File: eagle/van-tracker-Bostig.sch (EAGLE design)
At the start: 13 parts, among them K1 CP1-12V, Q1 TIP122

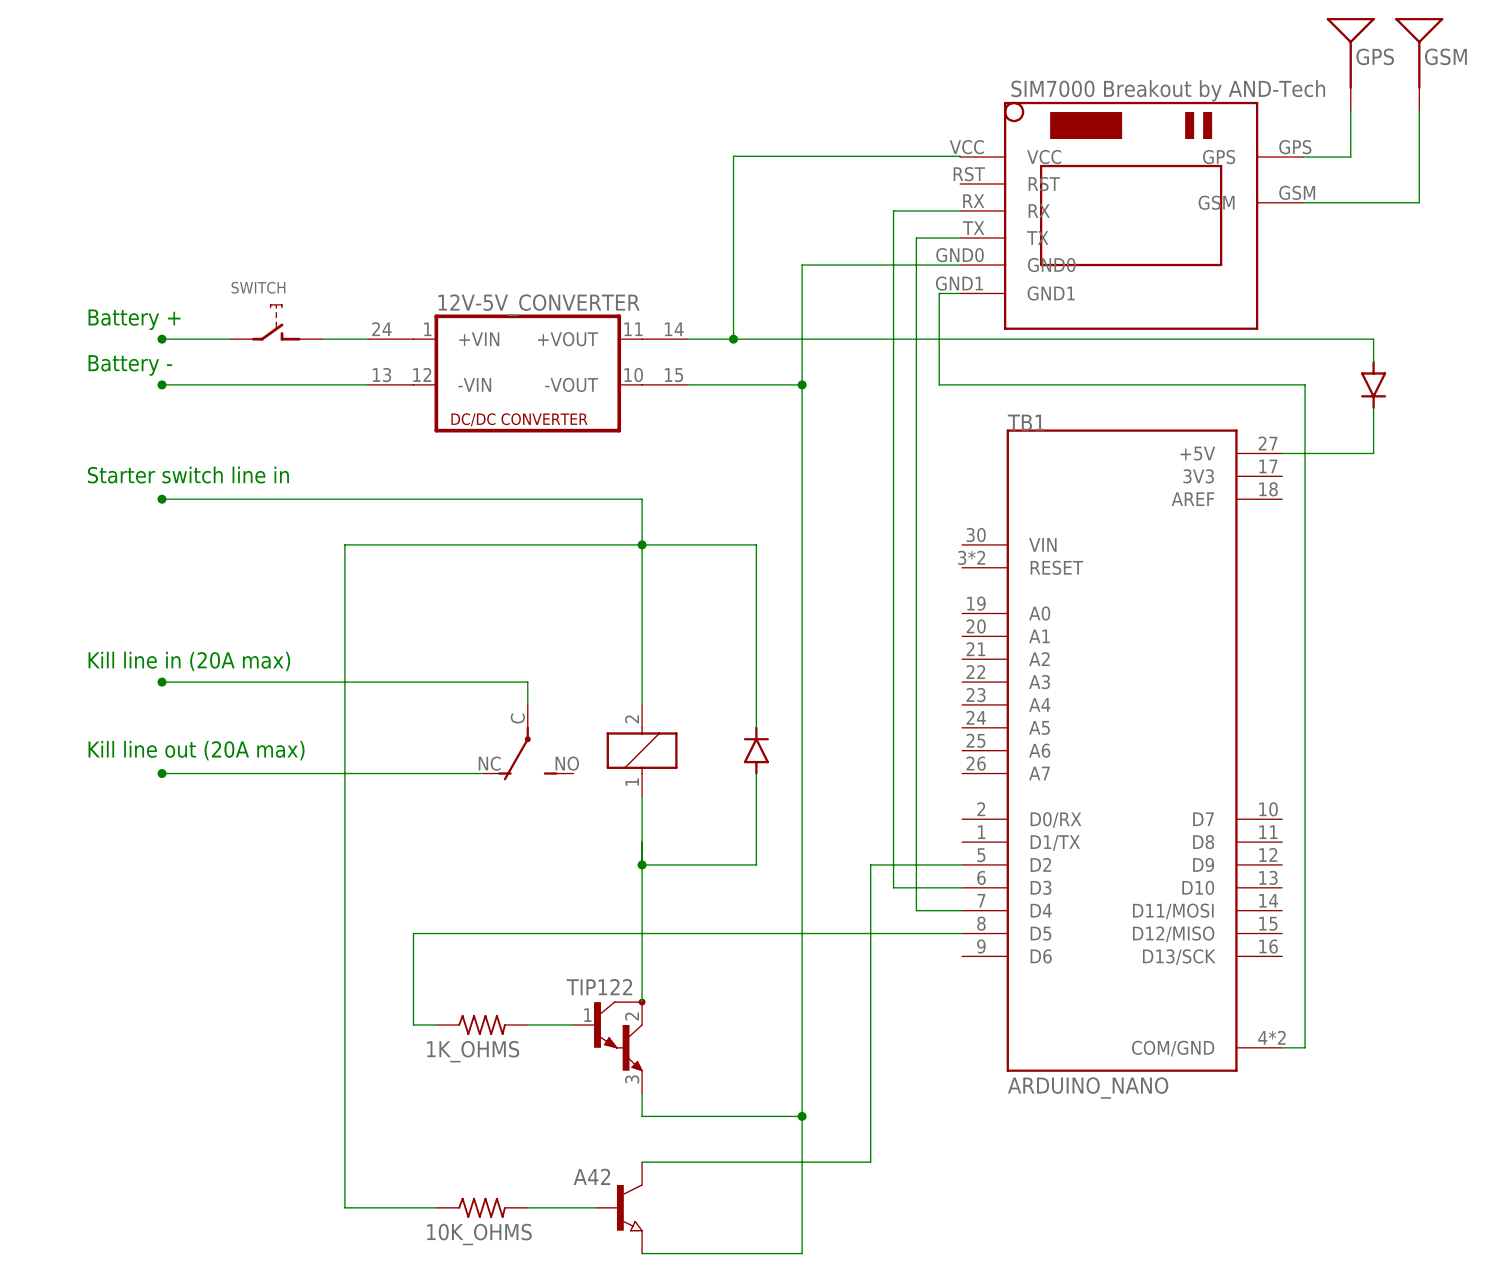
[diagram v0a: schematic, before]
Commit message: both bostig and stock: 1.change 10K resistor to 4M Ohm 2.make wiring look more like reality so building the hardware is more clear/intuitive including adding jumpers and inputs to PCB
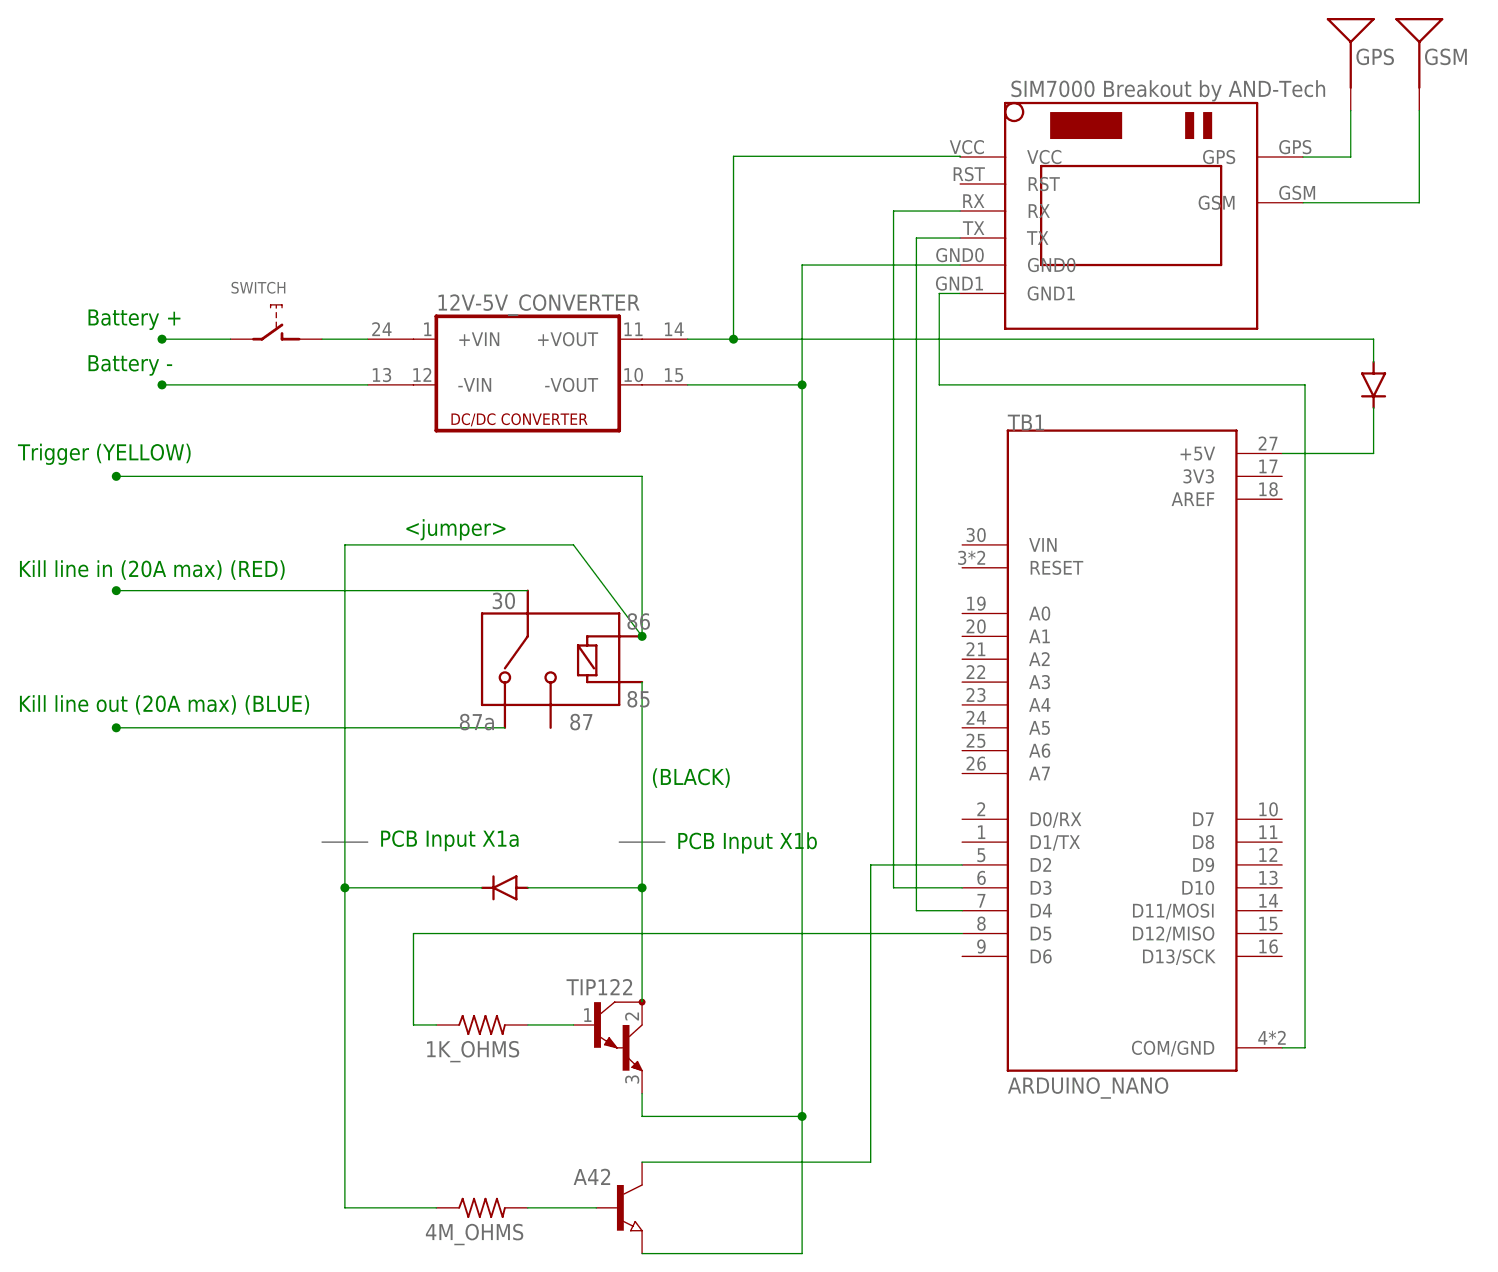
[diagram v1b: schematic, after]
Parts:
- removed K1: CP1-12V, relay:CP1-12V
- renumbered 10K_OHMS to 4M_OHMS
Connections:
- removed net N$7: K12.P
- removed net N$8: K12.O
- net N$17: now also D1.A, Q1.C; no longer 4M_OHMS.1, D1.C, K11.2
- net N$5: now also 4M_OHMS.1, D1.C; no longer D1.A, K11.1, Q1.C
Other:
- note added: "(BLACK)"
- note added: "<jumper>"
- note added: "Kill line in (20A max) (RED)"
- note added: "Kill line out (20A max) (BLUE)"
- note added: "PCB Input X1a"
- note added: "PCB Input X1b"
- note added: "Trigger (YELLOW)"
- note removed: "Kill line in (20A max)"
- note removed: "Kill line out (20A max)"
- note removed: "Starter switch line in"
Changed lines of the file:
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@@
 </groups>
 <parts>
-<part name="K1" library="relay" library_urn="urn:adsk.eagle:library:339" deviceset="CP1?-*" device="" package3d_urn="urn:adsk.eagle:package:24447/1" technology="12V"/>
 <part name="12V-5V_CONVERTER" library="dc-dc-converter" library_urn="urn:adsk.eagle:library:208" deviceset="DC213R" device="" package3d_urn="urn:adsk.eagle:package:12311/1"/>
 <part name="TB1" library="ARDUINO_NANO" deviceset="ARDUINO_NANO" device=""/>
@@
 <part name="Q1" library="transistor-npn" library_urn="urn:adsk.eagle:library:398" deviceset="TIP122*" device="" package3d_urn="urn:adsk.eagle:package:28520/1"/>
 <part name="D2" library="diode" library_urn="urn:adsk.eagle:library:210" deviceset="1N5400" device="" package3d_urn="urn:adsk.eagle:package:43365/2"/>
-<part name="10K_OHMS" library="rcl" library_urn="urn:adsk.eagle:library:334" deviceset="R-US_" device="0411/15" package3d_urn="urn:adsk.eagle:package:23568/2"/>
+<part name="4M_OHMS" library="rcl" library_urn="urn:adsk.eagle:library:334" deviceset="R-US_" device="0411/15" package3d_urn="urn:adsk.eagle:package:23568/2"/>
 <part name="A42" library="semicon-smd-ipc" library_urn="urn:adsk.eagle:library:353" deviceset="NPN-TRANSISTOR_" device="SOT23" package3d_urn="urn:adsk.eagle:package:28738/2"/>
+<part name="U$2" library="JW_RELAY01" deviceset="JW_RELAY_BOSCH01" device=""/>
 </parts>
 <sheets>
 <sheet>
 <plain>
-<text x="-41.402" y="29.464" size="1.778" layer="91">Kill line in (20A max)</text>
-<text x="-41.402" y="19.558" size="1.778" layer="91">Kill line out (20A max)</text>
-<text x="-41.402" y="50.038" size="1.778" layer="91">Starter switch line in</text>
+<text x="-49.022" y="39.624" size="1.778" layer="91">Kill line in (20A max) (RED)</text>
+<text x="-49.022" y="24.638" size="1.778" layer="91">Kill line out (20A max) (BLUE)</text>
+<text x="-49.022" y="52.578" size="1.778" layer="91">Trigger (YELLOW)</text>
 <text x="-41.402" y="67.564" size="1.778" layer="91">Battery +</text>
 <text x="-41.402" y="62.484" size="1.778" layer="91">Battery -</text>
+<text x="-6.096" y="44.196" size="1.778" layer="91">&lt;jumper&gt;</text>
+<text x="21.336" y="16.51" size="1.778" layer="91">(BLACK)</text>
+<text x="-8.89" y="9.652" size="1.778" layer="91">PCB Input X1a</text>
+<text x="24.13" y="9.398" size="1.778" layer="91">PCB Input X1b</text>
 </plain>
 <instances>
-<instance part="K1" gate="1" x="20.32" y="20.32" smashed="yes" rot="R180" grouprefs="RELAY"/>
-<instance part="K1" gate="2" x="7.62" y="22.86" smashed="yes" rot="R180" grouprefs="RELAY"/>
 <instance part="12V-5V_CONVERTER" gate="G$1" x="7.62" y="63.5" smashed="yes">
 <attribute name="NAME" x="-2.54" y="69.215" size="1.778" layer="95"/>
@@
 </instance>
 <instance part="U$1" gate="G$1" x="73.66" y="81.28" smashed="yes"/>
-<instance part="D1" gate="1" x="33.02" y="20.32" smashed="yes" rot="R90"/>
+<instance part="D1" gate="1" x="5.08" y="5.08" smashed="yes" rot="R180"/>
 <instance part="1K_OHMS" gate="G$1" x="2.54" y="-10.16" smashed="yes">
 <attribute name="NAME" x="-3.81" y="-13.7414" size="1.778" layer="95"/>
@@
 </instance>
 <instance part="D2" gate="1" x="101.6" y="60.96" smashed="yes" rot="R270"/>
-<instance part="10K_OHMS" gate="G$1" x="2.54" y="-30.48" smashed="yes">
+<instance part="4M_OHMS" gate="G$1" x="2.54" y="-30.48" smashed="yes">
 <attribute name="NAME" x="-3.81" y="-34.0614" size="1.778" layer="95"/>
 <attribute name="VALUE" x="-1.27" y="-33.782" size="1.778" layer="96"/>
@@
 <attribute name="VALUE" x="7.62" y="-25.4" size="1.778" layer="96"/>
 </instance>
+<instance part="U$2" gate="G$1" x="7.62" y="33.02" smashed="yes" rot="R180"/>
 </instances>
 <busses>
+<bus name="B$1">
+<segment>
+<wire x1="-15.24" y1="10.16" x2="-10.16" y2="10.16" width="0.762" layer="92"/>
+</segment>
+</bus>
+<bus name="B$2">
+<segment>
+<wire x1="17.78" y1="10.16" x2="22.86" y2="10.16" width="0.762" layer="92"/>
+</segment>
+</bus>
 </busses>
 <nets>
@@
 <net name="N$7" class="0">
 <segment>
-<pinref part="K1" gate="2" pin="P"/>
-<wire x1="7.62" y1="25.4" x2="7.62" y2="27.94" width="0.1524" layer="91"/>
-<wire x1="7.62" y1="27.94" x2="-33.02" y2="27.94" width="0.1524" layer="91"/>
-<junction x="-33.02" y="27.94"/>
-</segment>
-</net>
-<net name="N$8" class="0">
-<segment>
-<junction x="-33.02" y="17.78"/>
-<pinref part="K1" gate="2" pin="O"/>
-<wire x1="2.54" y1="17.78" x2="-33.02" y2="17.78" width="0.1524" layer="91"/>
+<wire x1="7.62" y1="38.1" x2="-38.1" y2="38.1" width="0.1524" layer="91"/>
+<junction x="-38.1" y="38.1"/>
 </segment>
 </net>
@@
 </segment>
 </net>
-<net name="N$17" class="0">
-<segment>
-<pinref part="K1" gate="1" pin="2"/>
-<wire x1="20.32" y1="43.18" x2="20.32" y2="25.4" width="0.1524" layer="91"/>
+<net name="N$5" class="0">
+<segment>
+<pinref part="4M_OHMS" gate="G$1" pin="1"/>
+<wire x1="-12.7" y1="-30.48" x2="-2.54" y2="-30.48" width="0.1524" layer="91"/>
 <pinref part="D1" gate="1" pin="C"/>
-<wire x1="33.02" y1="22.86" x2="33.02" y2="43.18" width="0.1524" layer="91"/>
-<wire x1="33.02" y1="43.18" x2="20.32" y2="43.18" width="0.1524" layer="91"/>
-<wire x1="20.32" y1="43.18" x2="20.32" y2="48.26" width="0.1524" layer="91"/>
-<junction x="20.32" y="43.18"/>
-<junction x="-33.02" y="48.26"/>
-<wire x1="20.32" y1="48.26" x2="-33.02" y2="48.26" width="0.1524" layer="91"/>
-<pinref part="10K_OHMS" gate="G$1" pin="1"/>
-<wire x1="-12.7" y1="-30.48" x2="-2.54" y2="-30.48" width="0.1524" layer="91"/>
-<wire x1="20.32" y1="43.18" x2="-12.7" y2="43.18" width="0.1524" layer="91"/>
-<wire x1="-12.7" y1="43.18" x2="-12.7" y2="-30.48" width="0.1524" layer="91"/>
-</segment>
-</net>
-<net name="N$5" class="0">
-<segment>
-<pinref part="K1" gate="1" pin="1"/>
-<wire x1="20.32" y1="15.24" x2="20.32" y2="7.62" width="0.1524" layer="91"/>
-<pinref part="D1" gate="1" pin="A"/>
-<wire x1="33.02" y1="17.78" x2="33.02" y2="7.62" width="0.1524" layer="91"/>
-<wire x1="33.02" y1="7.62" x2="20.32" y2="7.62" width="0.1524" layer="91"/>
-<junction x="20.32" y="7.62"/>
-<pinref part="Q1" gate="G$1" pin="C"/>
-<wire x1="20.32" y1="7.62" x2="20.32" y2="10.16" width="0.1524" layer="91"/>
-<wire x1="20.32" y1="7.62" x2="20.32" y2="-7.62" width="0.1524" layer="91"/>
+<wire x1="-12.7" y1="5.08" x2="-12.7" y2="-30.48" width="0.1524" layer="91"/>
+<wire x1="2.54" y1="5.08" x2="-12.7" y2="5.08" width="0.1524" layer="91"/>
+<wire x1="-12.7" y1="5.08" x2="-12.7" y2="43.18" width="0.1524" layer="91"/>
+<junction x="-12.7" y="5.08"/>
+<wire x1="-12.7" y1="43.18" x2="12.7" y2="43.18" width="0.1524" layer="91"/>
+<junction x="-38.1" y="50.8"/>
+<wire x1="20.32" y1="50.8" x2="20.32" y2="33.02" width="0.1524" layer="91"/>
+<wire x1="20.32" y1="50.8" x2="-38.1" y2="50.8" width="0.1524" layer="91"/>
+<wire x1="12.7" y1="43.18" x2="20.32" y2="33.02" width="0.1524" layer="91"/>
+<junction x="20.32" y="33.02"/>
 </segment>
 </net>
@@
 <net name="N$14" class="0">
 <segment>
-<pinref part="10K_OHMS" gate="G$1" pin="2"/>
+<pinref part="4M_OHMS" gate="G$1" pin="2"/>
 <pinref part="A42" gate="G$1" pin="B"/>
 <wire x1="7.62" y1="-30.48" x2="15.24" y2="-30.48" width="0.1524" layer="91"/>
@@
 </segment>
 </net>
+<net name="N$8" class="0">
+<segment>
+<wire x1="5.08" y1="22.86" x2="-38.1" y2="22.86" width="0.1524" layer="91"/>
+<junction x="-38.1" y="22.86"/>
+</segment>
+</net>
+<net name="N$17" class="0">
+<segment>
+<pinref part="D1" gate="1" pin="A"/>
+<pinref part="Q1" gate="G$1" pin="C"/>
+<wire x1="20.32" y1="5.08" x2="20.32" y2="-7.62" width="0.1524" layer="91"/>
+<wire x1="20.32" y1="27.94" x2="20.32" y2="5.08" width="0.1524" layer="91"/>
+<junction x="20.32" y="5.08"/>
+<wire x1="20.32" y1="5.08" x2="7.62" y2="5.08" width="0.1524" layer="91"/>
+</segment>
+</net>
